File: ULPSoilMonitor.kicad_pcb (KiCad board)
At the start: 2 copper layers, 27.1 x 76.2 mm, 62 parts, among them J1 Conn_01x03_Male, J2 Conn_01x03_Male, J3 Conn_01x03_Male, J4 Conn_01x03_Male, J5 Conn_01x03_Male, J6 Conn_01x03_Male, J7 USB_B_Micro, J8 BME280_(GYBMEP), Q1 BC807, Q2 MMDT3904, Q3 BC817, Q4 MMDT3904, SW1 RESET, U1 ESP32-WROOM-32, U2 MCP73123, U3 CP2102N-A01-GQFN28, U4 BME280

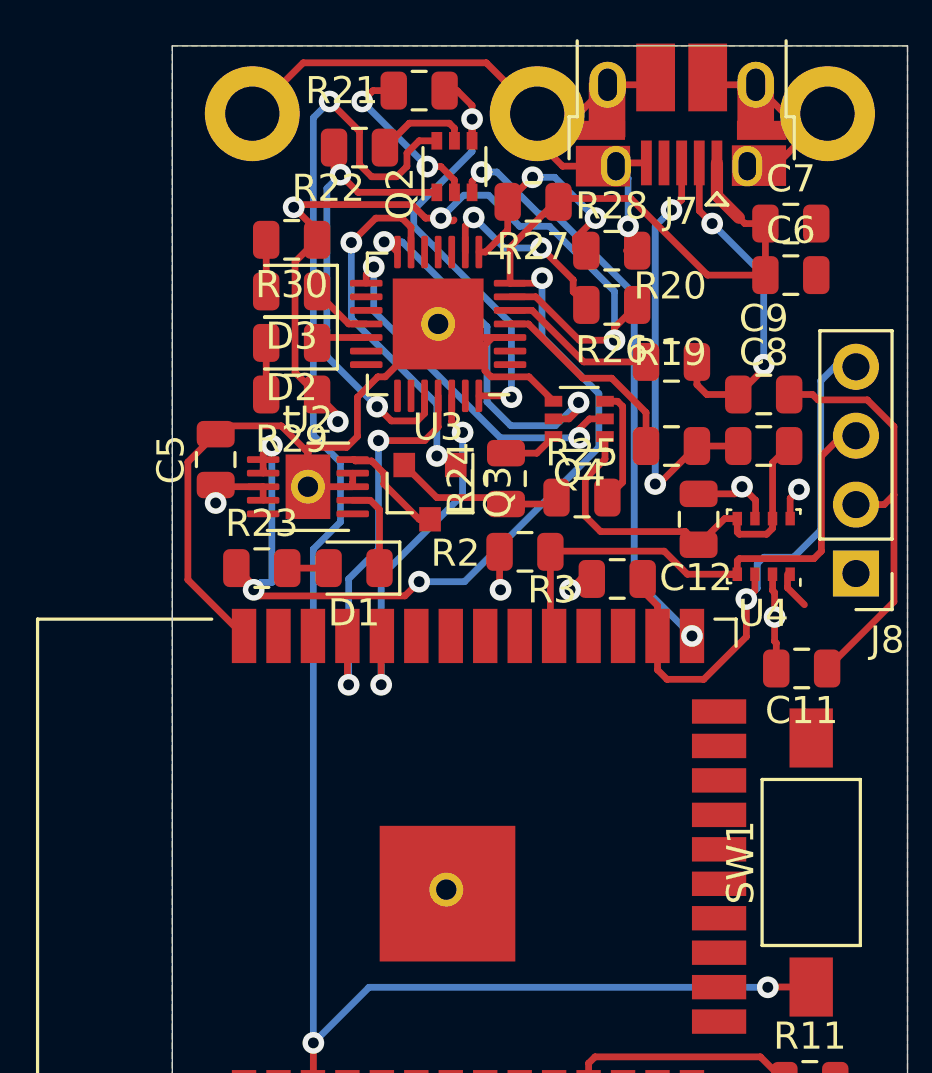
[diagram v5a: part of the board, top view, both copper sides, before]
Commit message: minor layout adjustments
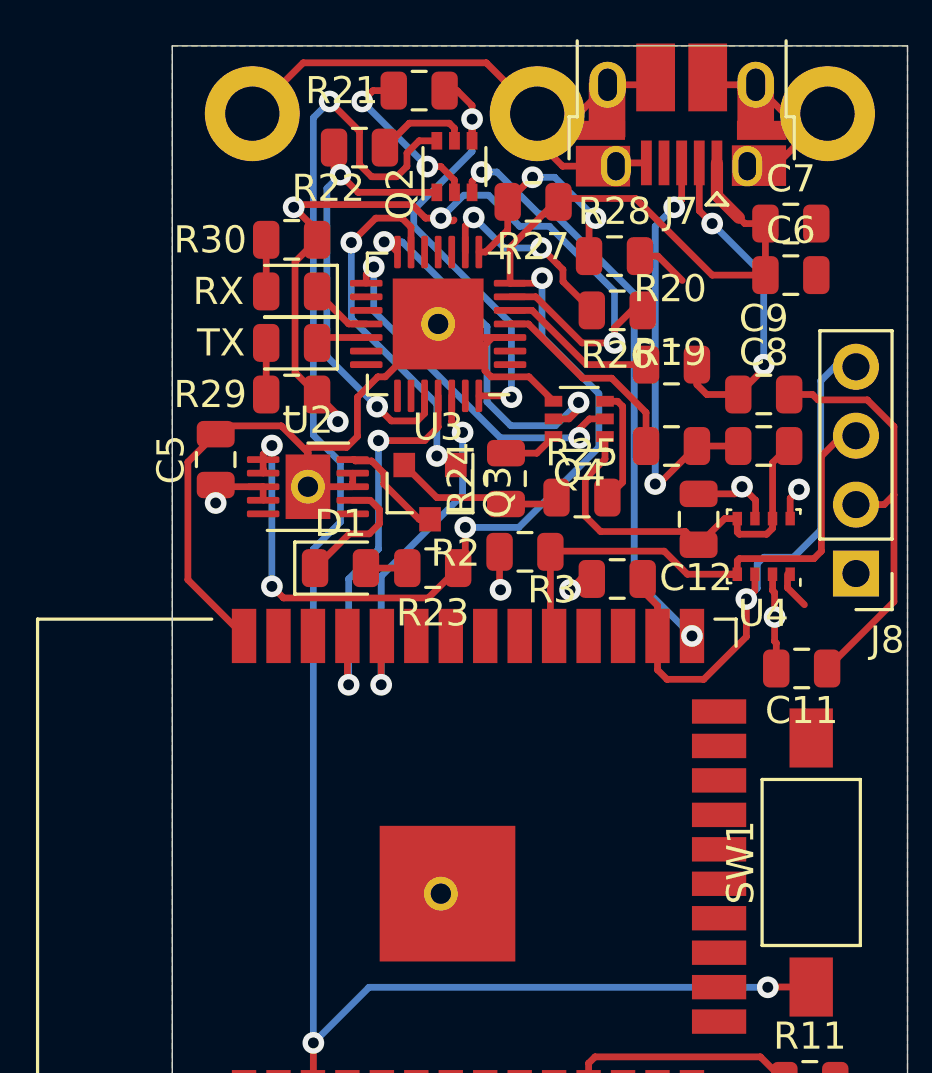
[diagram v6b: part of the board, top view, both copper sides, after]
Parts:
- removed D2: TX, LED_SMD:LED_0805_2012Metric
- added TX: TX, LED_SMD:LED_0805_2012Metric, F.Cu at (42.9, 39.2)
- moved R23 6.30 mm to (48.1, 47.5), turned to 180 degrees
- moved D1 0.50 mm to (44.7, 47.5), turned to 0 degrees
- moved R26 0.28 mm to (54.9, 38.0)
- moved R28 0.22 mm to (54.8, 36.0)
- moved R20 0.10 mm to (56.9, 40.0)
- renumbered D3 to RX
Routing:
- net Net-(D1-Pad1): track 3.29 -> 4.70 mm
- net -BATT: track 103.6 -> 102.2 mm, vias 1 -> 0
- net VBUS: track 49.5 -> 48.3 mm

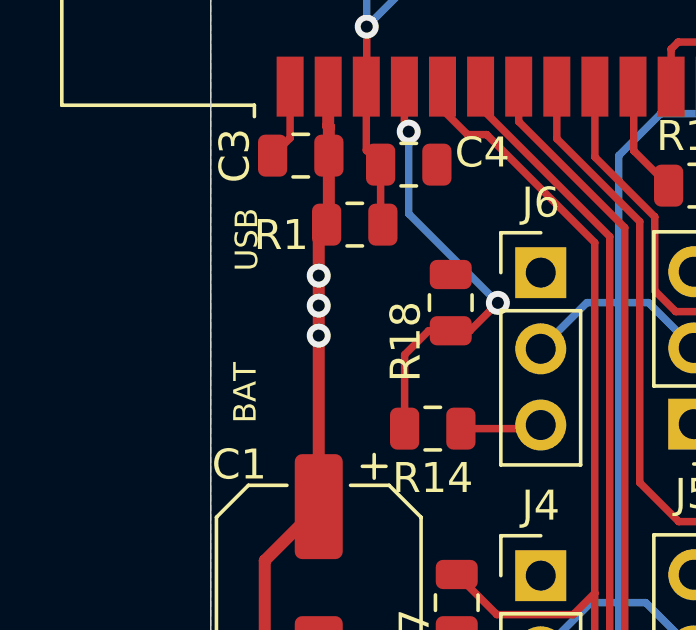
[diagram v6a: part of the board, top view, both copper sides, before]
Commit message: remove unused text
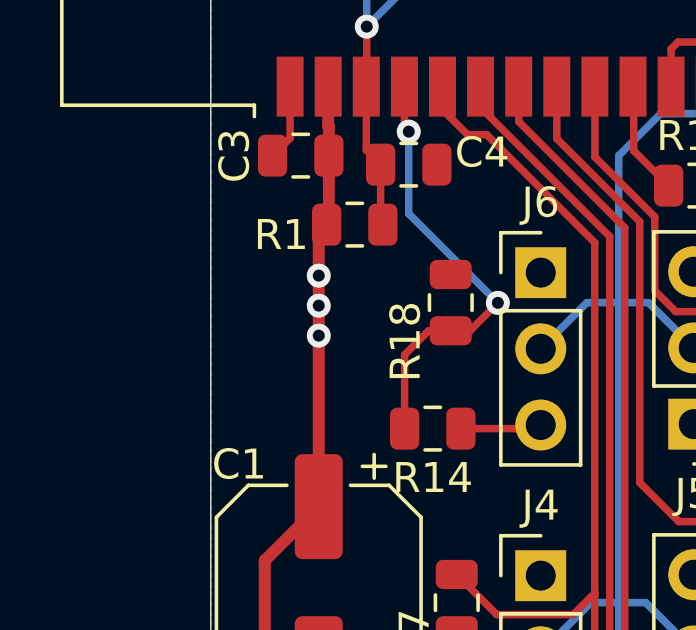
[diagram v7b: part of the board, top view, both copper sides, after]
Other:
- board text removed: "BAT"
- board text removed: "USB"
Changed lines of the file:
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@@
   (general
     (thickness 1.6)
-    (drawings 7)
+    (drawings 5)
     (tracks 553)
     (zones 0)
@@
     )
   )
-  (gr_text "BAT\n" (at 39.65 77.2 90) (layer F.SilkS)
-    (effects (font (size 0.75 0.75) (thickness 0.15)))
-  )
-  (gr_text USB (at 39.7 72.1 90) (layer F.SilkS)
-    (effects (font (size 0.75 0.75) (thickness 0.15)))
-  )
   (gr_text "Flobs ULPSoilMonitor v2.1\n2020-06-26" (at 63 85.8 90) (layer F.SilkS)

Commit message: update version
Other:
- board text added: "Flobs ULPSoilMonitor v2.2 2020-07-05"
- board text removed: "Flobs ULPSoilMonitor v2.1 2020-06-26"
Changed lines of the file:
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@@
   (title_block
     (title ULPSoilMonitor)
-    (date 2020-06-26)
-    (rev v2.1)
+    (date 2020-07-05)
+    (rev v2.2)
     (company Flobs)
   )
   (layers
-    (0 F.Cu signal)
-    (31 B.Cu signal)
+    (0 F.Cu signal hide)
+    (31 B.Cu signal hide)
     (32 B.Adhes user)
     (33 F.Adhes user)
@@
     )
   )
-  (gr_text "Flobs ULPSoilMonitor v2.1\n2020-06-26" (at 63 85.8 90) (layer F.SilkS)
+  (gr_text "Flobs ULPSoilMonitor v2.2\n2020-07-05" (at 63 85.8 90) (layer F.SilkS)
     (effects (font (size 1 1) (thickness 0.25)))
   )
